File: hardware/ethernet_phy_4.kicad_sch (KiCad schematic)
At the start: 29 parts, among them J3 RJMG1S8008101BR, SW2 SW TACT-SPST, U2 DP83826IRHBR, Y2 ABM8G-25.000MHZ-9-B4Y-T

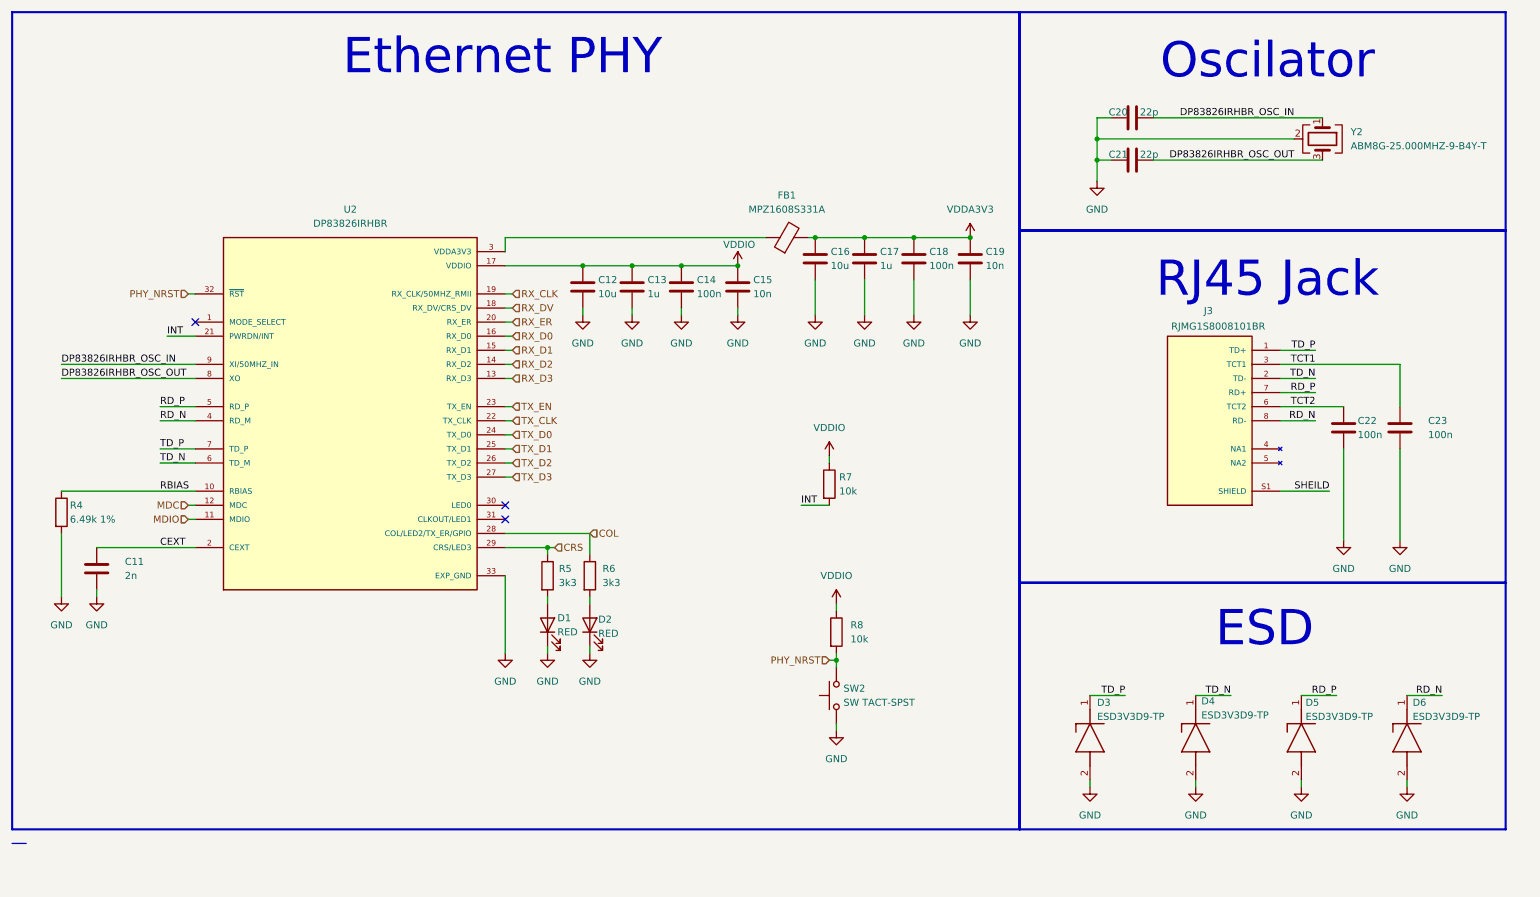
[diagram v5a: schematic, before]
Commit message: Place Components for Ethernet
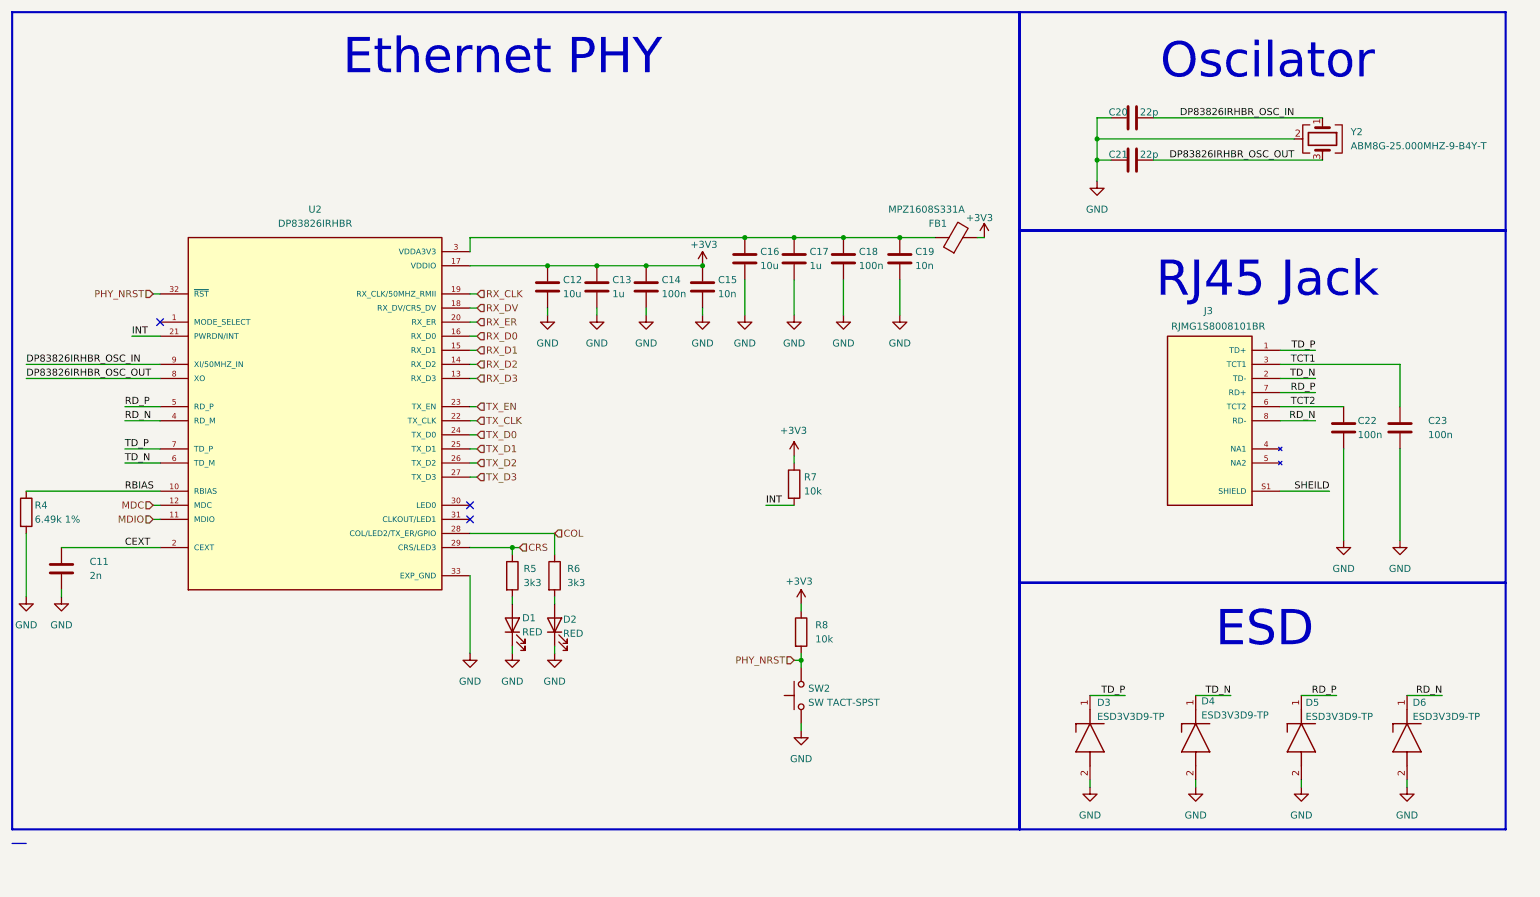
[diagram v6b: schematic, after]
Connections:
- net at FB1.1, U2.3 (VDDA3V3): now also C16.1, C17.1, C18.1, C19.1
- removed net VDDA3V3: C16.1, C17.1, C18.1, C19.1, FB1.2
- net VDDIO renamed +3V3
- net +3V3: now also FB1.2
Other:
- moved on the sheet: C11, C12, C13, C14, C15, C16, C17, C18, C19, D1, D2, R4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

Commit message: Place components for STM32F103 Programmer/Debugger
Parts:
- D1, D2: footprint STM32F407 Dev Kit Library:LED_1206_3216Metric_Pad1.42x1.75mm_HandSolder -> STM32F407 Dev Kit Library:LED_0805_2012Metric_Pad1.15x1.40mm_HandSolder
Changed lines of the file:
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@@
 			)
 		)
-		(property "Footprint" "STM32F407 Dev Kit Library:LED_1206_3216Metric_Pad1.42x1.75mm_HandSolder"
+		(property "Footprint" "STM32F407 Dev Kit Library:LED_0805_2012Metric_Pad1.15x1.40mm_HandSolder"
 			(at 113.03 127 0)
 			(hide yes)
@@
 			)
 		)
-		(property "Footprint" "STM32F407 Dev Kit Library:LED_1206_3216Metric_Pad1.42x1.75mm_HandSolder"
+		(property "Footprint" "STM32F407 Dev Kit Library:LED_0805_2012Metric_Pad1.15x1.40mm_HandSolder"
 			(at 105.41 127 0)
 			(hide yes)

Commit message: Place components for Power section
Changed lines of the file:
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@@
 	(wire
 		(pts
-			(xy 243.84 102.87) (xy 252.73 102.87)
+			(xy 243.84 102.87) (xy 245.11 102.87)
 		)
 		(stroke
@@
 		)
 	)
-	(label "SHEILD"
-		(at 252.73 102.87 180)
-		(effects
-			(font
-				(size 1.27 1.27)
-			)
-			(justify right bottom)
-		)
-	)
 	(label "TD_N"
 		(at 35.56 97.79 0)
@@
 		)
 	)
+	(hierarchical_label "SHEILD"
+		(shape input)
+		(at 245.11 102.87 0)
+		(effects
+			(font
+				(size 1.27 1.27)
+			)
+			(justify left)
+		)
+	)
